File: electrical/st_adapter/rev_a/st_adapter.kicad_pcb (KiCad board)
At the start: 2 copper layers, 40 x 24.6 mm, 2 parts, among them CN1 STADAPTER;M2x4RA, CN2 STLINK;4xF1x2+F1x4+F1x6

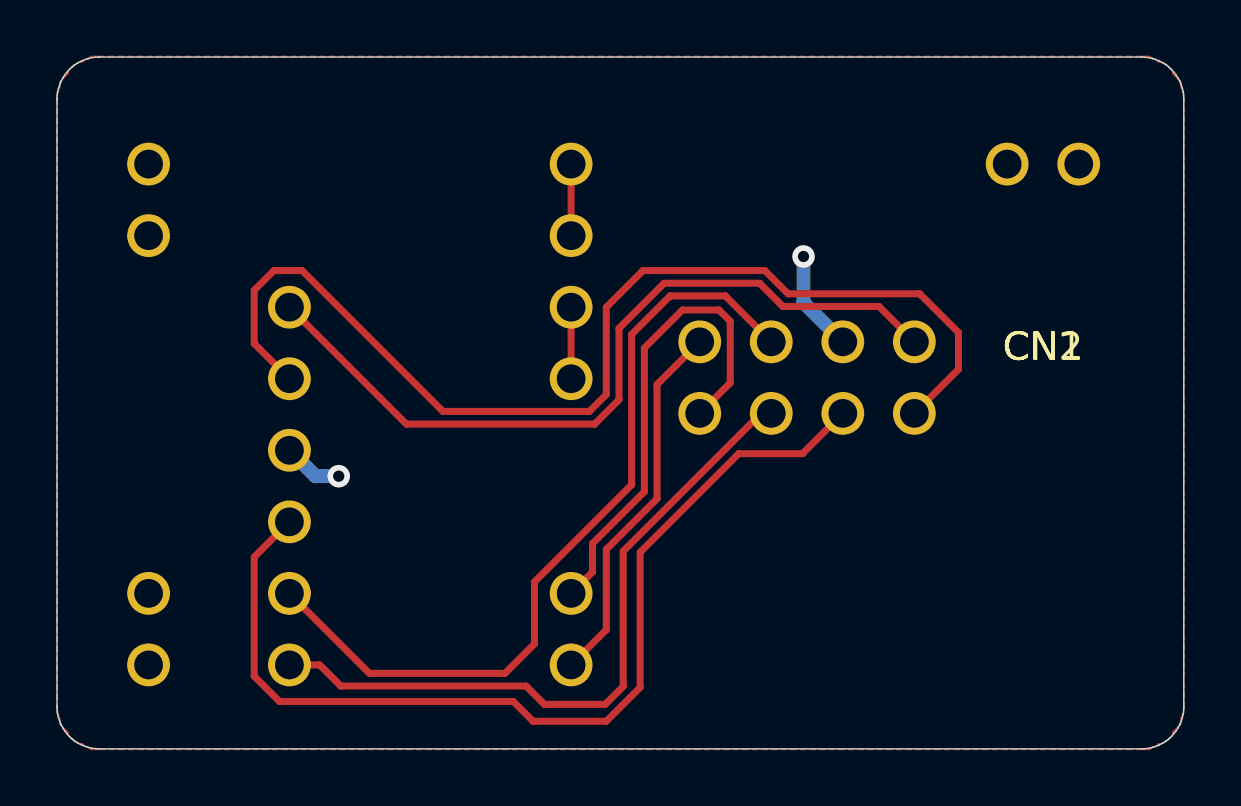
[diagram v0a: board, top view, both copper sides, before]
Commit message: Changes to encoder and st_adapter
Changed AH1806 symbol in encoder.sch
Changed resistor sizes in encoder sch and pcb
Kicad migrated st_adapter sch to new format
Added part designations to st_adapter pcb
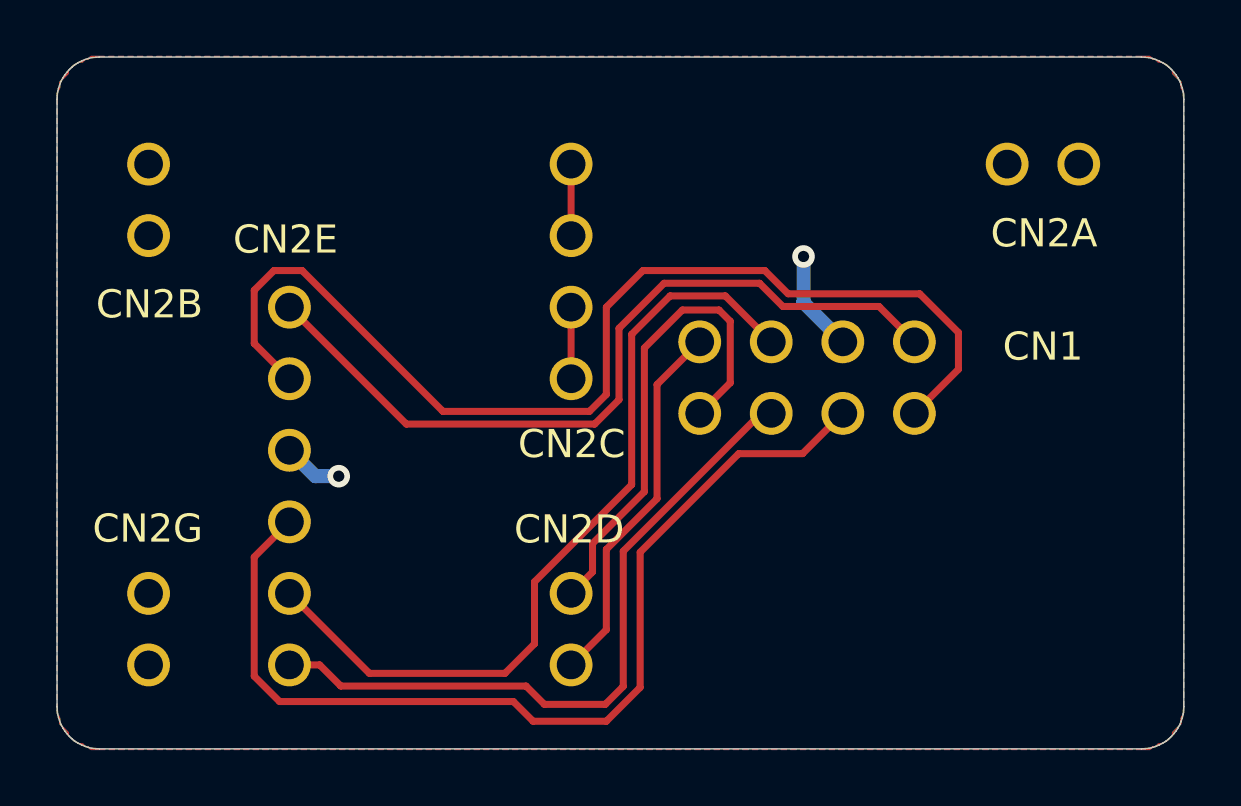
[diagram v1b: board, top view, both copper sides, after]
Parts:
- renumbered CN2 to CN2A
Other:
- board text added: "CN2B"
- board text added: "CN2C"
- board text added: "CN2D"
- board text added: "CN2E"
- board text added: "CN2G"

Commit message: Genereated gerbers for ST Adapter and Encoder.
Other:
- board text added: "HR2 ST ADAPTER Copyright © 2019-20 Homebrew Robotics Club License: MIT Date: 2020Dec26 Rev. A"
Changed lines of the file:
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@@
-(kicad_pcb (version 20171130) (host pcbnew 5.1.8-db9833491~88~ubuntu20.04.1)
+(kicad_pcb (version 20171130) (host pcbnew 5.1.9-73d0e3b20d~88~ubuntu20.04.1)
   (general
     (thickness 1.6)
-    (drawings 81)
+    (drawings 82)
     (tracks 75)
     (zones 0)
@@
       (outputformat 1)
       (mirror false)
-      (drillshape 1)
+      (drillshape 0)
       (scaleselection 1)
-      (outputdirectory ""))
+      (outputdirectory "./"))
   )
   (net 0 "")
@@
       (net 8 /3V3))
   )
+  (gr_text "HR2 ST ADAPTER\nCopyright © 2019-20 Homebrew Robotics Club\nLicense: MIT\nDate: 2020Dec26 Rev. A" (at 102.87 103.886) (layer B.SilkS)
+    (effects (font (size 0.75 0.75) (thickness 0.15)) (justify left mirror))
+  )
   (gr_text CN2G (at 68.22 104.46) (layer F.SilkS)
